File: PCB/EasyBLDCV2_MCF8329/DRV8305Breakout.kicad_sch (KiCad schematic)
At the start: 39 parts, among them Q1 CSD16556Q5B, Q2 CSD16556Q5B, Q3 CSD16556Q5B, Q4 CSD16556Q5B, Q5 CSD16556Q5B, Q6 CSD16556Q5B, U1 DRV83053PHP, U3 TPD4E05U06DQAR

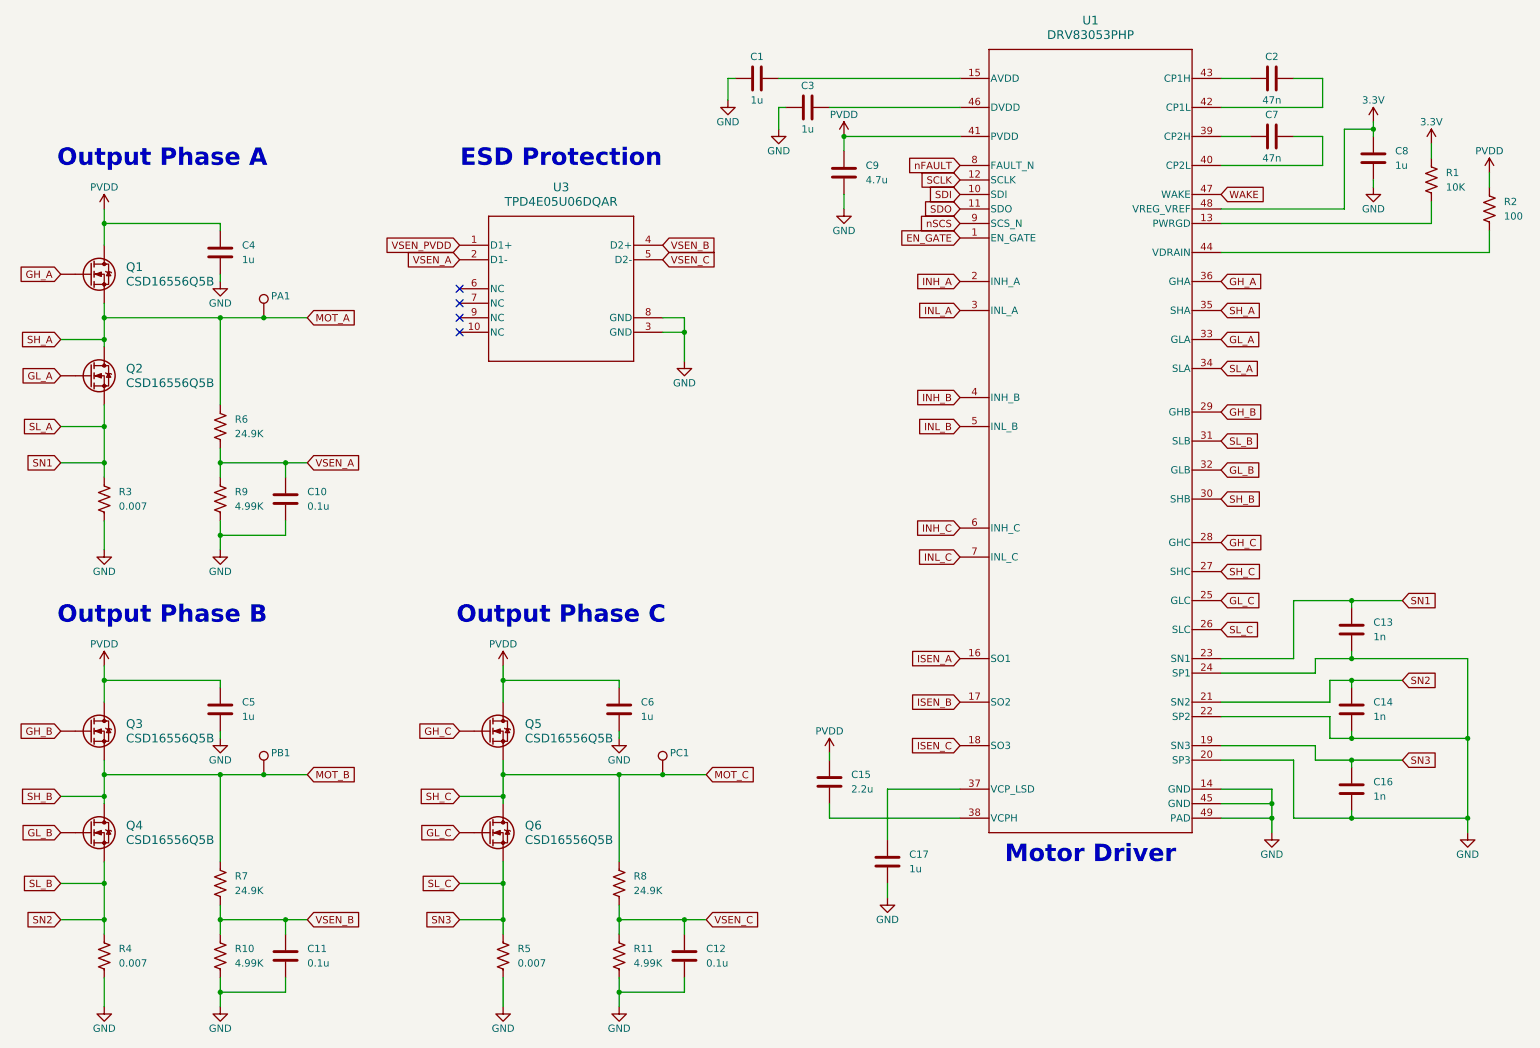
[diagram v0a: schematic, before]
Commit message: Deleted V1 Relics, redid power stage
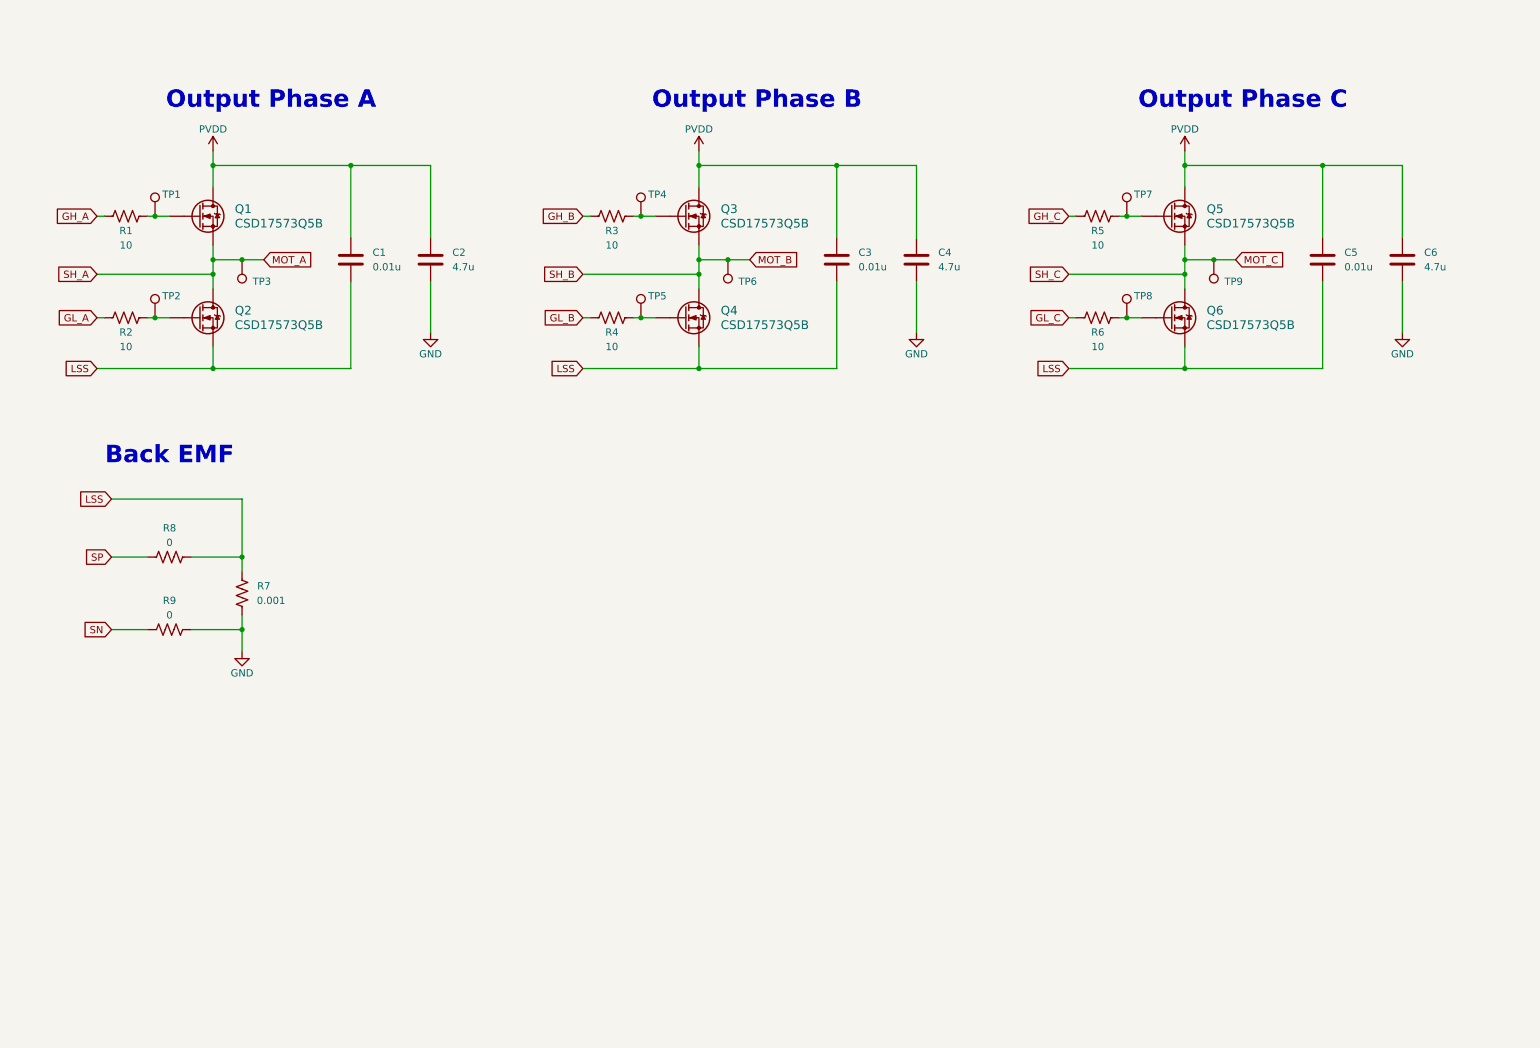
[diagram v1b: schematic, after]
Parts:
- removed C1, C17, C8: 1u, Capacitor_SMD:C_0603_1608Metric, symbol Device:C
- removed C10, C11, C12: 0.1u, Capacitor_SMD:C_0402_1005Metric, symbol Device:C
- removed C13, C14, C16: 1n, Capacitor_SMD:C_0402_1005Metric, symbol Device:C
- removed C15: 2.2u, Capacitor_SMD:C_0603_1608Metric, symbol Device:C
- removed C7: 47n, Capacitor_SMD:C_0603_1608Metric, symbol Device:C
- removed C9: 4.7u, Capacitor_SMD:C_0603_1608Metric, symbol Device:C
- removed PA1, PB1, PC1: TestPoint, TestPoint:TestPoint_Pad_D2.0mm, symbol Connector:TestPoint
- removed Q1, Q2, Q3, Q4, Q5, Q6: CSD16556Q5B, EasyBLDC:DNK0008A, symbol EasyBLDC:CSD16556Q5B
- removed R10, R11: 4.99K, Resistor_SMD:R_0402_1005Metric, symbol Device:R_US
- removed U1: DRV83053PHP, EasyBLDC:PHP0048G_N, symbol EasyBLDC:DRV83053PHP
- removed U3: TPD4E05U06DQAR, EasyBLDC:DQA0010A, symbol EasyBLDC:TPD4E05U06DQAR
- added C4: 4.7u, Capacitor_SMD:C_0603_1608Metric, symbol Device:C
- added Q1, Q2, Q3, Q4, Q5, Q6: CSD17573Q5B, DNK0008A, symbol EasyBLDC:CSD17573Q5B
- added TP1, TP2, TP3, TP4, TP5, TP6, TP7, TP8, TP9: TestPoint, symbol Connector:TestPoint
- C1: renamed from C4; value 1u -> 0.01u
- C2: value 47n -> 4.7u
- C3, C5: value 1u -> 0.01u
- C6: value 1u -> 4.7u
- R1: value 10K -> 10; footprint Fuse:Fuse_0603_1608Metric -> Resistor_SMD:R_2512_6332Metric
- R2: value 100 -> 10; footprint Fuse:Fuse_0603_1608Metric -> Resistor_SMD:R_2512_6332Metric
- R3, R4, R5: value 0.007 -> 10
- R6: value 24.9K -> 10; footprint Resistor_SMD:R_0603_1608Metric -> Resistor_SMD:R_2512_6332Metric
- R7: value 24.9K -> 0.001; footprint Resistor_SMD:R_0603_1608Metric -> Resistor_SMD:R_2512_6332Metric
- R8: value 24.9K -> 0; footprint Resistor_SMD:R_0603_1608Metric -> Resistor_SMD:R_2512_6332Metric
- R9: value 4.99K -> 0; footprint Resistor_SMD:R_0402_1005Metric -> Resistor_SMD:R_2512_6332Metric
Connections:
- net 3.3V is gone; now on net GH_A: R1.1
- net SL_A is gone; now on net GH_B: R3.1
- net SL_B is gone; now on net GL_B: R4.1
- net SL_C is gone; now on net GH_C: R5.1
- net VSEN_B is gone; now on net LSS: R7.2
- net GL_A: now also R2.1
- net GL_C: now also R6.1
- net GND: now also C2.2, R7.1, R9.1, C4.2; no longer C1.2, C3.1, C5.2, R3.2, R4.2, R5.2, R9.2
- net MOT_A: now also Q1.1 (S), Q1.2 (S), Q1.3 (S), Q2.5 (D), Q2.6 (D), Q2.7 (D), Q2.8 (D), TP3.1; no longer R6.1
- net MOT_B: now also Q3.1 (S), Q3.2 (S), Q3.3 (S), Q4.5 (D), Q4.6 (D), Q4.7 (D), Q4.8 (D), TP6.1; no longer R7.1
- net MOT_C: now also Q5.1 (S), Q5.2 (S), Q5.3 (S), Q6.5 (D), Q6.6 (D), Q6.7 (D), Q6.8 (D), TP9.1; no longer R8.1
- net PVDD: now also C2.1, C3.1, C4.1, Q1.5 (D), Q1.6 (D), Q1.7 (D), Q1.8 (D), Q3.5 (D), Q3.6 (D), Q3.7 (D), Q3.8 (D), Q5.5 (D), Q5.6 (D), Q5.7 (D), Q5.8 (D); no longer R2.1
- net at R1.2: now also Q1.4 (G), TP1.1
- net at R2.2: now also Q2.4 (G), TP2.1
- net LSS: now reaches C3.2
- net LSS: now also C1.2, C5.2, R8.1, Q2.1 (S), Q2.2 (S), Q2.3 (S), Q4.1 (S), Q4.2 (S), Q4.3 (S), Q6.1 (S), Q6.2 (S), Q6.3 (S)
- net VSEN_A: no longer names the net of R6.2
- net VSEN_A: now also Q6.4 (G), TP8.1; no longer R9.1
- net VSEN_C renamed SP
- new net: Q5.4 (G), R5.2, TP7.1
- new net: Q3.4 (G), R3.2, TP4.1
- new net: Q4.4 (G), R4.2, TP5.1
- new net SN: R9.2
- no-connect marks 4 -> 0
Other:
- note added: "Back EMF"
- note removed: "ESD Protection"
- note removed: "Motor Driver"
- title: Easy ESC -> Easy BLDC
- moved on the sheet: C1

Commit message: Finished schematic
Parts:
- C1, C2, C3, C4, C5, C6: footprint Capacitor_SMD:C_0603_1608Metric -> (none)
- Q1, Q2, Q3, Q4, Q5, Q6: footprint DNK0008A -> EasyBLDC:DNK0008A
- R1, R2, R3, R4, R5, R6, R7, R8, R9: footprint Resistor_SMD:R_2512_6332Metric -> (none)
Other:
- note added: "Current Sense"
- note removed: "Back EMF"
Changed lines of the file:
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@@
 		)
 	)
-	(text "Back EMF\n"
+	(text "Current Sense\n"
 		(exclude_from_sim no)
 		(at 45.72 90.17 0)
@@
 			)
 		)
-		(property "Footprint" "Resistor_SMD:R_2512_6332Metric"
+		(property "Footprint" ""
 			(at 38.354 65.024 90)
 			(effects
@@
 			)
 		)
-		(property "Footprint" "Resistor_SMD:R_2512_6332Metric"
+		(property "Footprint" ""
 			(at 208.534 65.024 90)
 			(effects
@@
 			)
 		)
-		(property "Footprint" "DNK0008A"
+		(property "Footprint" "EasyBLDC:DNK0008A"
 			(at 230.378 51.562 0)
 			(effects
@@
 			)
 		)
-		(property "Footprint" "Resistor_SMD:R_2512_6332Metric"
+		(property "Footprint" ""
 			(at 123.444 47.244 90)
 			(effects
@@
 			)
 		)
-		(property "Footprint" "Capacitor_SMD:C_0603_1608Metric"
+		(property "Footprint" ""
 			(at 248.6152 59.69 0)
 			(effects
@@
 			)
 		)
-		(property "Footprint" "Resistor_SMD:R_2512_6332Metric"
+		(property "Footprint" ""
 			(at 38.354 47.244 90)
 			(effects
@@
 			)
 		)
-		(property "Footprint" "Capacitor_SMD:C_0603_1608Metric"
+		(property "Footprint" ""
 			(at 92.4052 59.69 0)
 			(effects
@@
 			)
 		)
-		(property "Footprint" "Resistor_SMD:R_2512_6332Metric"
+		(property "Footprint" ""
 			(at 45.466 108.966 90)
 			(effects
@@
 			)
 		)
-		(property "Footprint" "DNK0008A"
+		(property "Footprint" "EasyBLDC:DNK0008A"
 			(at 145.288 69.342 0)
 			(effects
@@
 			)
 		)
-		(property "Footprint" "DNK0008A"
+		(property "Footprint" "EasyBLDC:DNK0008A"
 			(at 230.378 69.342 0)
 			(effects
@@
 			)
 		)
-		(property "Footprint" "DNK0008A"
+		(property "Footprint" "EasyBLDC:DNK0008A"
 			(at 60.198 69.342 0)
 			(effects
@@
 			)
 		)
-		(property "Footprint" "Capacitor_SMD:C_0603_1608Metric"
+		(property "Footprint" ""
 			(at 177.4952 59.69 0)
 			(effects
@@
 			)
 		)
-		(property "Footprint" "DNK0008A"
+		(property "Footprint" "EasyBLDC:DNK0008A"
 			(at 60.198 51.562 0)
 			(effects
@@
 			)
 		)
-		(property "Footprint" "Capacitor_SMD:C_0603_1608Metric"
+		(property "Footprint" ""
 			(at 78.4352 59.69 0)
 			(effects
@@
 			)
 		)
-		(property "Footprint" "Resistor_SMD:R_2512_6332Metric"
+		(property "Footprint" ""
 			(at 123.444 65.024 90)
 			(effects
@@
 			)
 		)
-		(property "Footprint" "Resistor_SMD:R_2512_6332Metric"
+		(property "Footprint" ""
 			(at 57.404 114.046 90)
 			(effects
@@
 			)
 		)
-		(property "Footprint" "Capacitor_SMD:C_0603_1608Metric"
+		(property "Footprint" ""
 			(at 163.5252 59.69 0)
 			(effects
@@
 			)
 		)
-		(property "Footprint" "Resistor_SMD:R_2512_6332Metric"
+		(property "Footprint" ""
 			(at 45.466 121.666 90)
 			(effects
@@
 			)
 		)
-		(property "Footprint" "Resistor_SMD:R_2512_6332Metric"
+		(property "Footprint" ""
 			(at 208.534 47.244 90)
 			(effects
@@
 			)
 		)
-		(property "Footprint" "DNK0008A"
+		(property "Footprint" "EasyBLDC:DNK0008A"
 			(at 145.288 51.562 0)
 			(effects
@@
 			)
 		)
-		(property "Footprint" "Capacitor_SMD:C_0603_1608Metric"
+		(property "Footprint" ""
 			(at 262.5852 59.69 0)
 			(effects

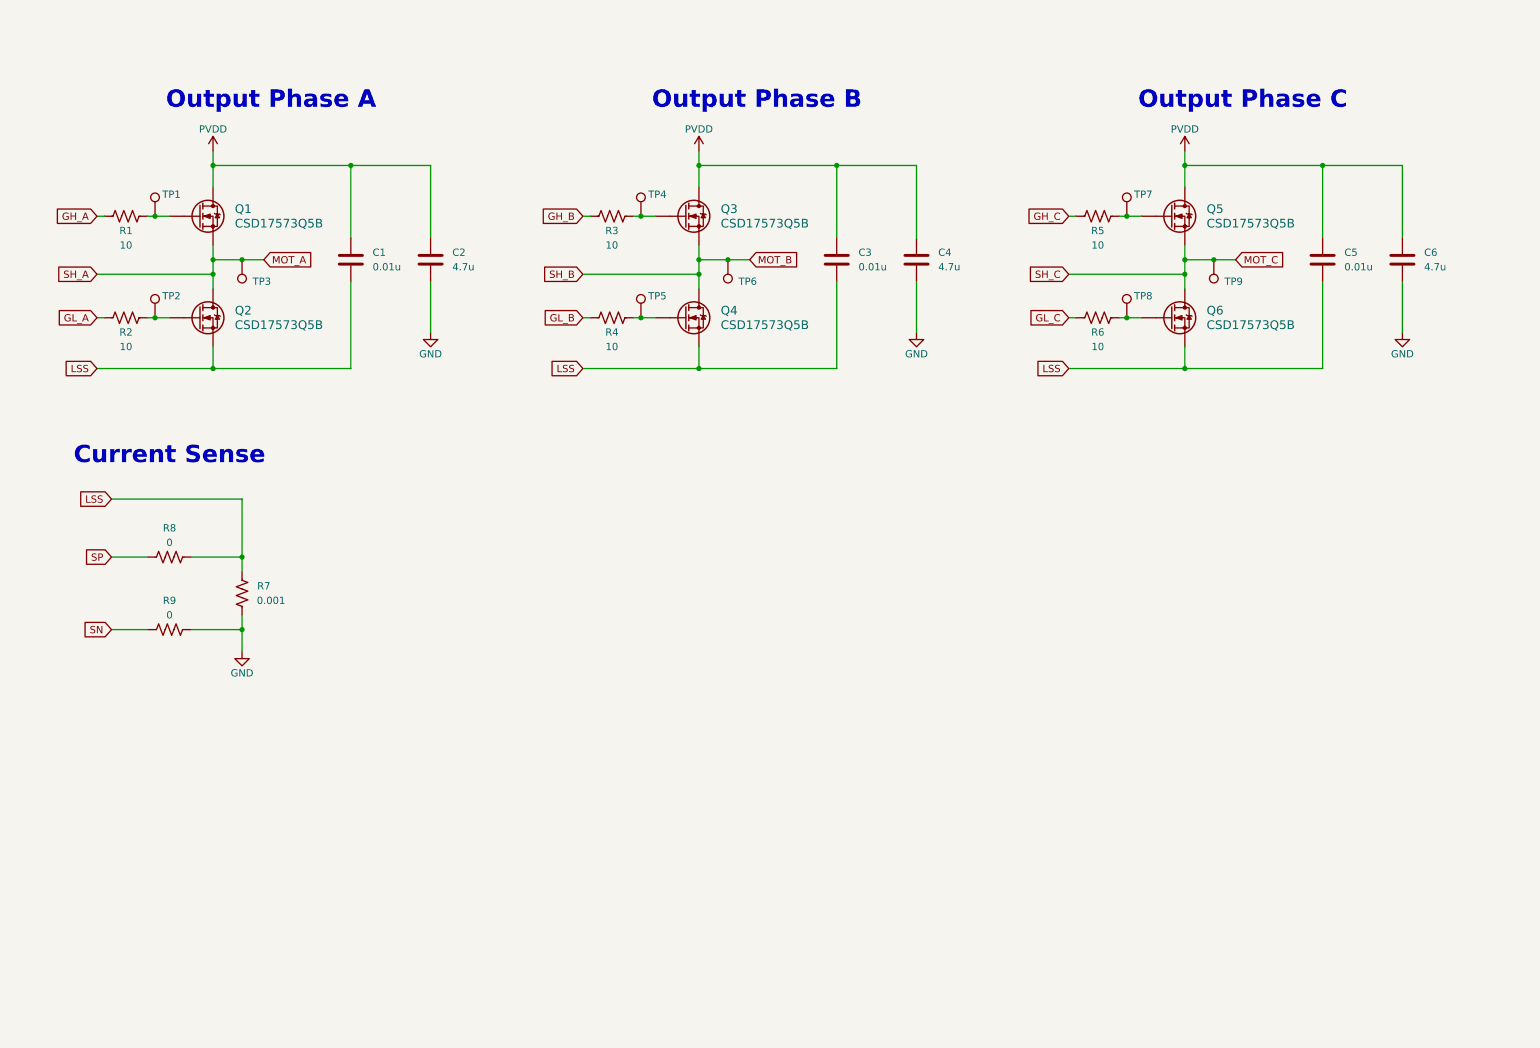
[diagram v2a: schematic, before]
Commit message: Assigned footprints, created bom
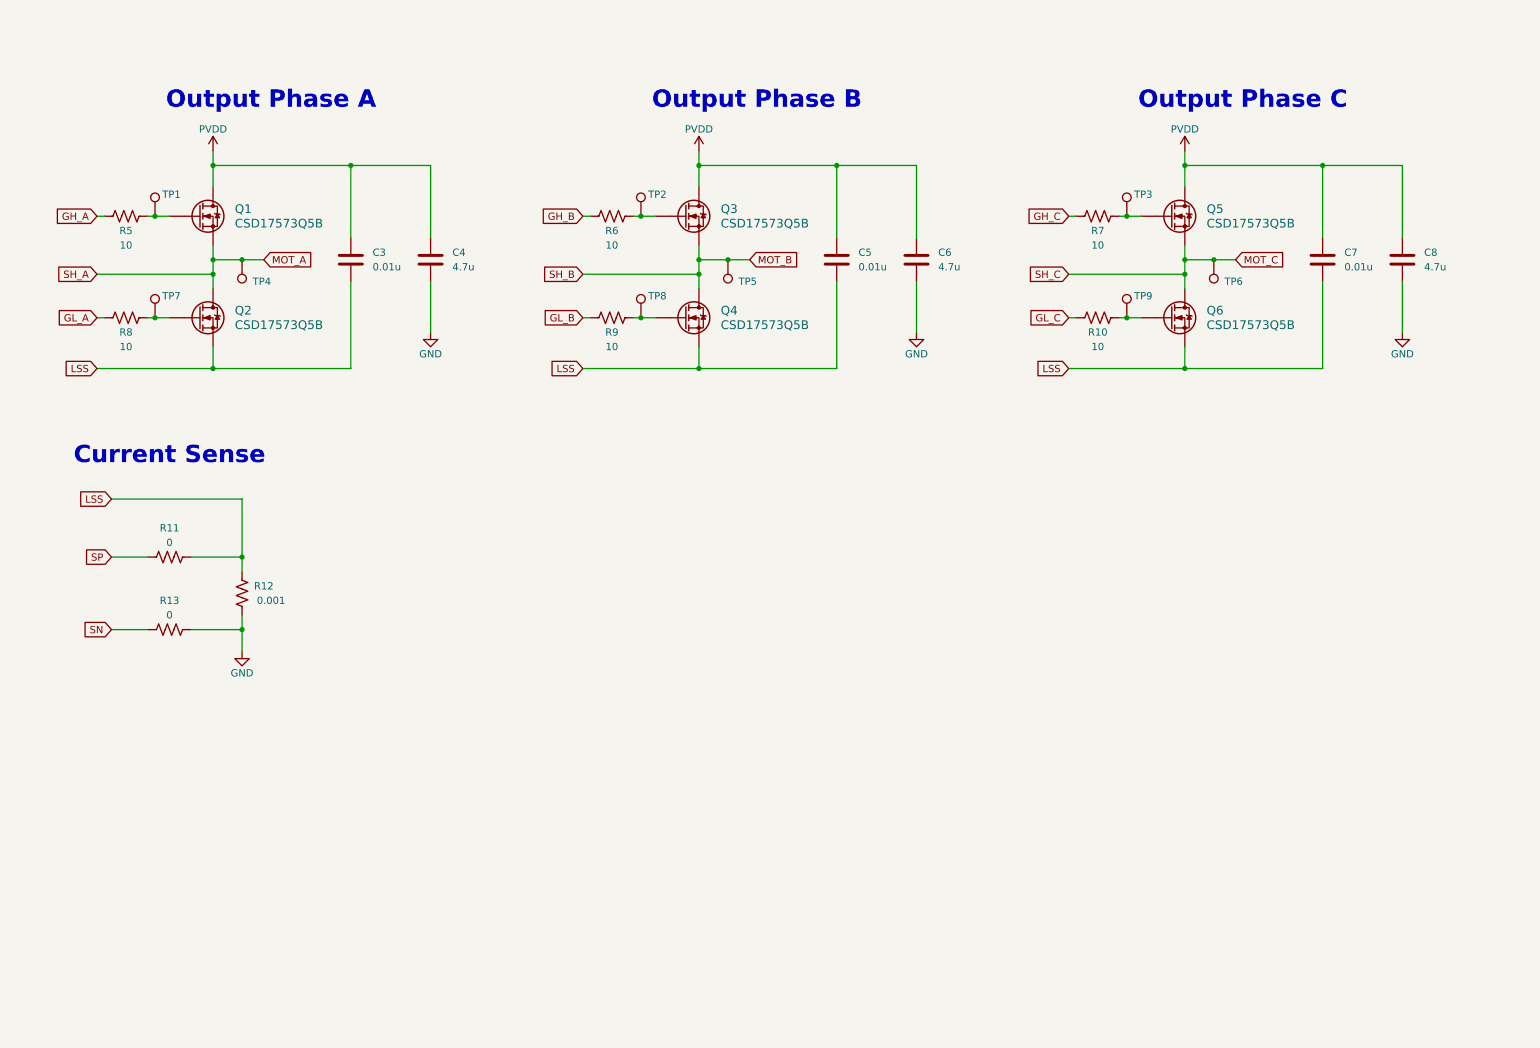
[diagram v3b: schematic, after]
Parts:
- C3: renamed from C1; footprint (none) -> Capacitor_SMD:C_0805_2012Metric
- C4: renamed from C2; footprint (none) -> Capacitor_SMD:C_1210_3225Metric
- C5: renamed from C3; footprint (none) -> Capacitor_SMD:C_0805_2012Metric
- C6: renamed from C4; footprint (none) -> Capacitor_SMD:C_1210_3225Metric
- C7: renamed from C5; footprint (none) -> Capacitor_SMD:C_0805_2012Metric
- C8: renamed from C6; footprint (none) -> Capacitor_SMD:C_1210_3225Metric
- R10: renamed from R6; footprint (none) -> Resistor_SMD:R_0603_1608Metric
- R11: renamed from R8; footprint (none) -> Resistor_SMD:R_0603_1608Metric
- R12: renamed from R7; footprint (none) -> Resistor_SMD:R_0603_1608Metric
- R13: renamed from R9; footprint (none) -> Resistor_SMD:R_0603_1608Metric
- R5: renamed from R1; footprint (none) -> Resistor_SMD:R_0603_1608Metric
- R6: renamed from R3; footprint (none) -> Resistor_SMD:R_0603_1608Metric
- R7: renamed from R5; footprint (none) -> Resistor_SMD:R_0603_1608Metric
- R8: renamed from R2; footprint (none) -> Resistor_SMD:R_0603_1608Metric
- R9: renamed from R4; footprint (none) -> Resistor_SMD:R_0603_1608Metric
- TP1: footprint (none) -> TestPoint:TestPoint_Pad_D1.5mm
- TP2: renamed from TP4; footprint (none) -> TestPoint:TestPoint_Pad_D1.5mm
- TP3: renamed from TP7; footprint (none) -> TestPoint:TestPoint_Pad_D1.5mm
- TP4: renamed from TP3; footprint (none) -> TestPoint:TestPoint_Pad_D1.5mm
- TP5: renamed from TP6; footprint (none) -> TestPoint:TestPoint_Pad_D1.5mm
- TP6: renamed from TP9; footprint (none) -> TestPoint:TestPoint_Pad_D1.5mm
- TP7: renamed from TP2; footprint (none) -> TestPoint:TestPoint_Pad_D1.5mm
- TP8: renamed from TP5; footprint (none) -> TestPoint:TestPoint_Pad_D1.5mm
- TP9: renamed from TP8; footprint (none) -> TestPoint:TestPoint_Pad_D1.5mm

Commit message: Redid Power Fills
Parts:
- R12: footprint Resistor_SMD:R_0603_1608Metric -> Resistor_SMD:R_2512_6332Metric
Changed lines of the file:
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@@
 			)
 		)
-		(property "Footprint" "Resistor_SMD:R_0603_1608Metric"
+		(property "Footprint" "Resistor_SMD:R_2512_6332Metric"
 			(at 57.404 114.046 90)
 			(effects
